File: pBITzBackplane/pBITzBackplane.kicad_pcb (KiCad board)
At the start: 4 copper layers, 243.8 x 243.8 mm, 53 parts, among them J1 ATX-24, J2 pBITzBus, J3 pBITzBus, J4 pBITzBus, J5 pBITzBus, J6 pBITzBus, J7 Conn_02x10_Odd_Even, Q1 BSS138, SW1 SW_Push, U1 ATtiny85-20P

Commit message: Changed the pBITz backplane connector from a PCIe 8x to a DIN 41612 connector.
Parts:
- removed H1: MountingHole, MountingHole:MountingHole_3.5mm_Pad_TopBottom
- removed H10, H11, H12, H13: MountingHole (DB), MountingHole:MountingHole_3.5mm_Pad_TopBottom
- removed H2: MountingHole (C), MountingHole:MountingHole_3.5mm_Pad_TopBottom
- removed H3: MountingHole (J), MountingHole:MountingHole_3.5mm_Pad_TopBottom
- removed H4: MountingHole (S), MountingHole:MountingHole_3.5mm_Pad_TopBottom
- removed H5: MountingHole (R), MountingHole:MountingHole_3.5mm_Pad_TopBottom
- removed H6: MountingHole (B), MountingHole:MountingHole_3.5mm_Pad_TopBottom
- removed H7: MountingHole (M), MountingHole:MountingHole_3.5mm_Pad_TopBottom
- removed H8: MountingHole (H), MountingHole:MountingHole_3.5mm_Pad_TopBottom
- removed H9: MountingHole (L), MountingHole:MountingHole_3.5mm_Pad_TopBottom
- removed J2, J3, J4, J5: pBITzBus, Footprints:AMPHENOL_10018783-10202TLF
- removed RN1, RN2: 4820P-2-472LF, Footprints:SOIC127P762X240-20N
- removed RN3, RN4: 4816P-T02-472LF, Footprints:4816PT02472LF
- added H14: MountingHole_Pad (D), MountingHole:MountingHole_3.5mm_Pad_TopBottom, F.Cu at (182.8, 198.1)
- added H15: MountingHole_Pad (J), MountingHole:MountingHole_3.5mm_Pad_TopBottom, F.Cu at (386.0, 353.1)
- added H16: MountingHole_Pad (R), MountingHole:MountingHole_3.5mm_Pad_TopBottom, F.Cu at (182.8, 353.1)
- added H17: MountingHole_Pad (M), MountingHole:MountingHole_3.5mm_Pad_TopBottom, F.Cu at (293.1, 352.7)
- added H18: MountingHole_Pad (L), MountingHole:MountingHole_3.5mm_Pad_TopBottom, F.Cu at (293.1, 424.1)
- added H19: MountingHole_Pad (DB), MountingHole:MountingHole_3.5mm_Pad_TopBottom, F.Cu at (228.5, 198.1)
- added H20: MountingHole_Pad (DB), MountingHole:MountingHole_3.5mm_Pad_TopBottom, F.Cu at (386.0, 425.4)
- added H21: MountingHole_Pad (C), MountingHole:MountingHole_3.5mm_Pad_TopBottom, F.Cu at (202.2, 352.7)
- added H22: MountingHole_Pad (S), MountingHole:MountingHole_3.5mm_Pad_TopBottom, F.Cu at (228.5, 425.4)
- added H23: MountingHole_Pad (B), MountingHole:MountingHole_3.5mm_Pad_TopBottom, F.Cu at (202.2, 424.1)
- added H24: MountingHole_Pad (H), MountingHole:MountingHole_3.5mm_Pad_TopBottom, F.Cu at (386.0, 221.0)
- added H25: MountingHole_Pad (DB), MountingHole:MountingHole_3.5mm_Pad_TopBottom, F.Cu at (162.5, 353.1)
- added H26: MountingHole_Pad (DB), MountingHole:MountingHole_3.5mm_Pad_TopBottom, F.Cu at (228.5, 353.1)
- added J10: ~, Footprints:AMPHENOL_86093968114T55F1LF, F.Cu at (184.8, 282.5)
- added J11: ~, Footprints:AMPHENOL_86093968114T55F1LF, F.Cu at (164.5, 282.5)
- added J8: ~, Footprints:AMPHENOL_86093968114T55F1LF, F.Cu at (225.5, 282.5)
- added J9: ~, Footprints:AMPHENOL_86093968114T55F1LF, F.Cu at (205.2, 282.5)
- added RN10: 4614X-101-472LF, Resistor_THT:R_Array_SIP14, F.Cu at (240.7, 289.7)
- added RN5: 4614X-101-472LF, Resistor_THT:R_Array_SIP14, F.Cu at (234.3, 253.4)
- added RN6: 4614X-101-472LF, Resistor_THT:R_Array_SIP14, F.Cu at (237.5, 253.4)
- added RN7: 4614X-101-472LF, Resistor_THT:R_Array_SIP14, F.Cu at (240.7, 253.4)
- added RN8: 4614X-101-472LF, Resistor_THT:R_Array_SIP14, F.Cu at (234.3, 289.7)
- added RN9: 4614X-101-472LF, Resistor_THT:R_Array_SIP14, F.Cu at (237.5, 289.7)
- moved C15 55.7 mm to (221.6, 233.0)
- moved C12 46.3 mm to (160.6, 233.0)
- moved C14 25.9 mm to (201.3, 233.0)
- moved J7 13.6 mm to (250.8, 341.4)
- moved C13 7.06 mm to (180.9, 233.0)
- moved C8 5.69 mm to (167.6, 233.0), turned to 0 degrees
- moved C9 5.67 mm to (187.9, 233.0), turned to 0 degrees
- moved C10 5.66 mm to (208.2, 233.0), turned to 0 degrees
- moved C11 5.58 mm to (228.5, 233.0), turned to 0 degrees
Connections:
- net /Backplane/SPI_CD renamed /Backplane/~{SPI_CD}
- net /Backplane/SPI_CS0 renamed /Backplane/~{SPI_CS0}
- net /Backplane/SPI_CS1 renamed /Backplane/~{SPI_CS1}
- J6 pad A5: /Backplane/CLK2 -> unconnected-(J6A-CLK2-PadA5)
- J6 pad A6: /Backplane/CLK3 -> unconnected-(J6A-CLK3-PadA6)
- J6 pad A8: /Backplane/PROG -> /Backplane/~{PROG}
- J6 pad B8: /Backplane/CART -> /Backplane/~{CART}
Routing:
- net /Backplane/CART: track 197.8 -> 0.00 mm, vias 2 -> 0
- net /Backplane/PROG: track 191.3 -> 0.00 mm, vias 2 -> 0
- net /Backplane/~{PROG}: track 0.00 -> 169.6 mm, vias 0 -> 1
- net /Backplane/~{CART}: track 0.00 -> 161.1 mm, vias 0 -> 2
- net /Backplane/CLK3: track 138.2 -> 0.00 mm, vias 1 -> 0
- net /Backplane/CLK2: track 136.6 -> 0.00 mm, vias 1 -> 0
- net +3V3: track 544.4 -> 594.9 mm
- net /Backplane/~{SHUTDOWN_RQ}: track 314.6 -> 359.4 mm, vias 1 -> 2
- net /Backplane/~{PWR_OFF}: track 323.2 -> 360.7 mm, vias 1 -> 2
- net /Backplane/CTRL_2: track 206.1 -> 168.7 mm, vias 2 -> 0
- net /Backplane/CTRL_5: track 208.3 -> 171.9 mm, vias 2 -> 0
- net /Backplane/CTRL_1: track 204.5 -> 169.6 mm, vias 2 -> 1
- net /Backplane/A22: track 234.4 -> 267.5 mm, vias 2 -> 1
- net /Backplane/A21: track 235.2 -> 268.1 mm, vias 2 -> 1
- net /Backplane/~{RESET}: track 202.0 -> 169.6 mm, vias 2 -> 1
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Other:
- board text added: "Mezzanine Card When attached to backplane use Holes H17, H18, H21, H23"
- board text removed: "3V3"
- board text removed: "5V"
- board text removed: "A12"
- board text removed: "A20"
- board text removed: "A23"
- board text removed: "CS2"
- board text removed: "CTRL0"
- board text removed: "CTRL11"
- board text removed: "CTRL19"
- board text removed: "CTRL9"
- board text removed: "D15"
- board text removed: "D8"
- board text removed: "Mezzanine Card When attached to backplane use Holes H10-H13"
- board text removed: "Mezzanine Connector"
- board text removed: "SPI"

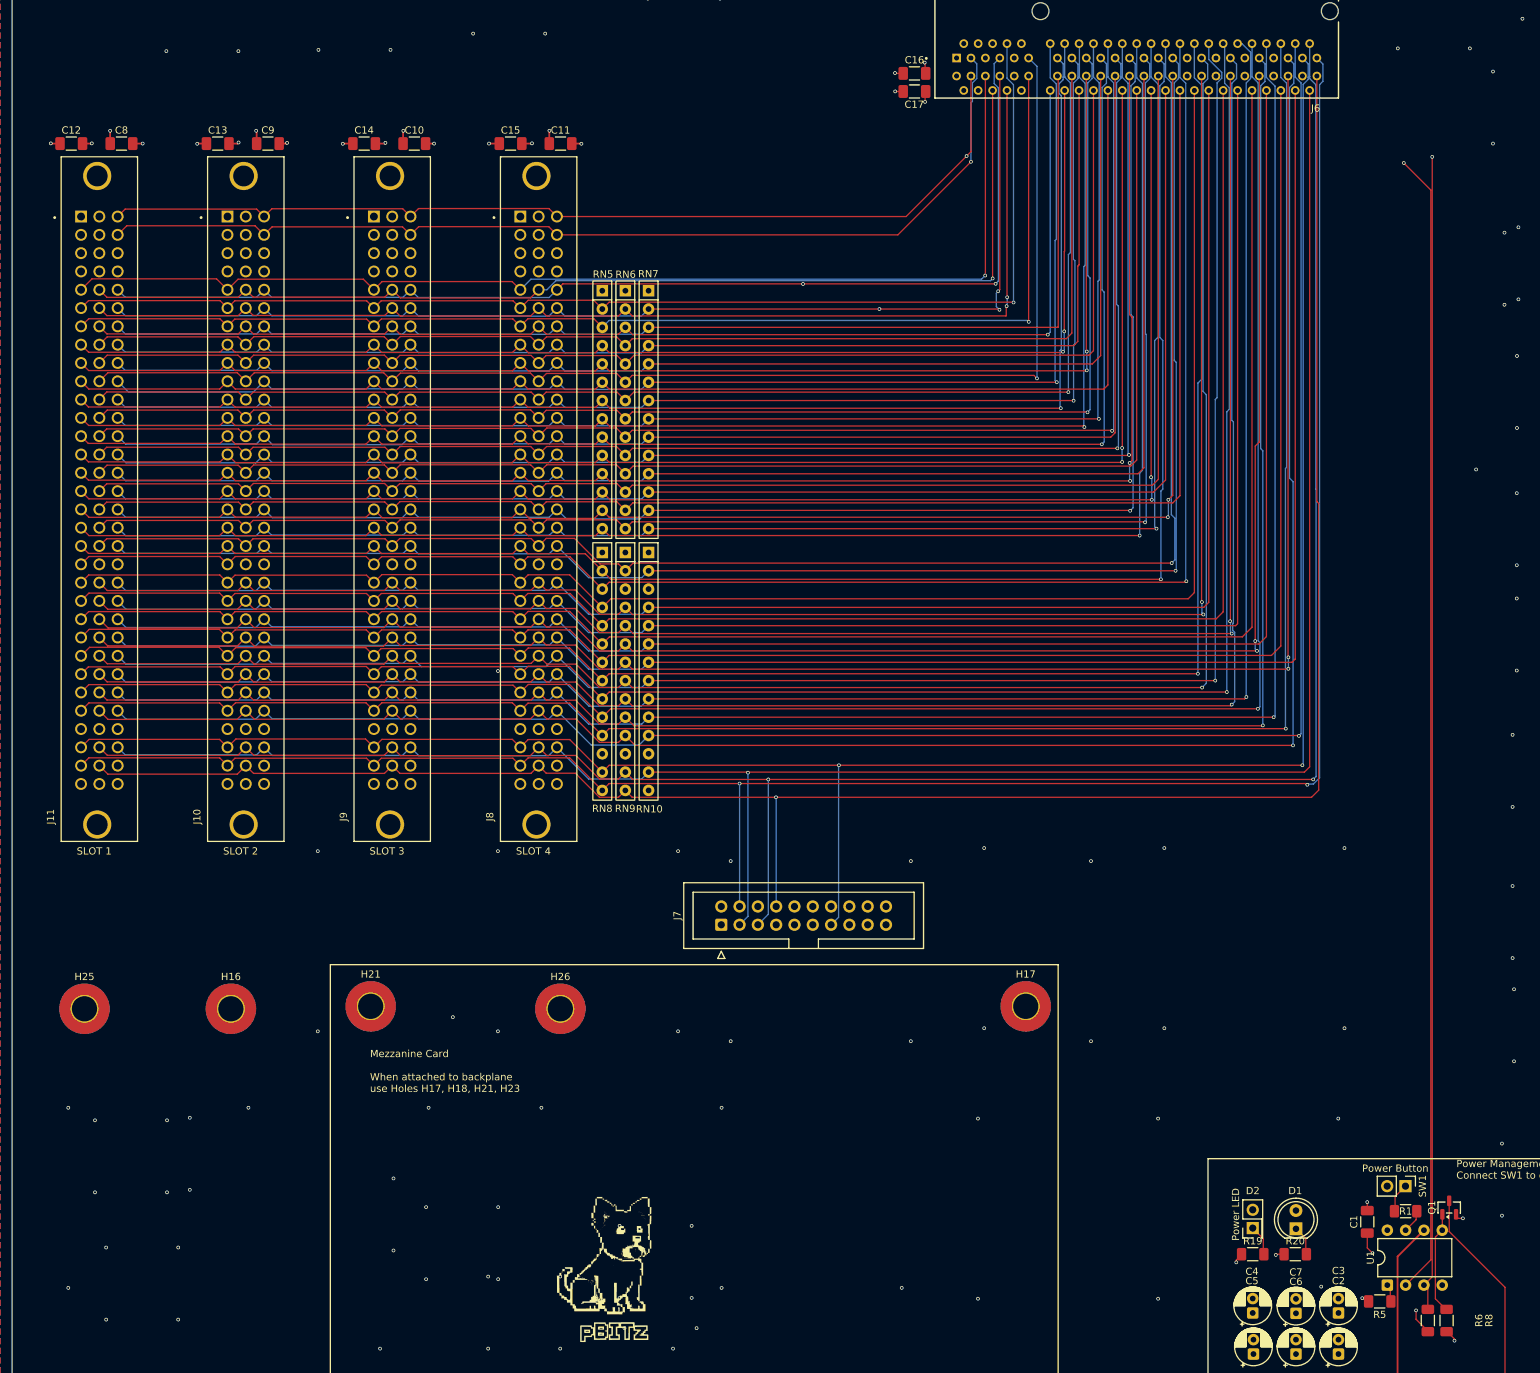
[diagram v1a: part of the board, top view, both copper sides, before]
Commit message: Moved to the DIN Connector
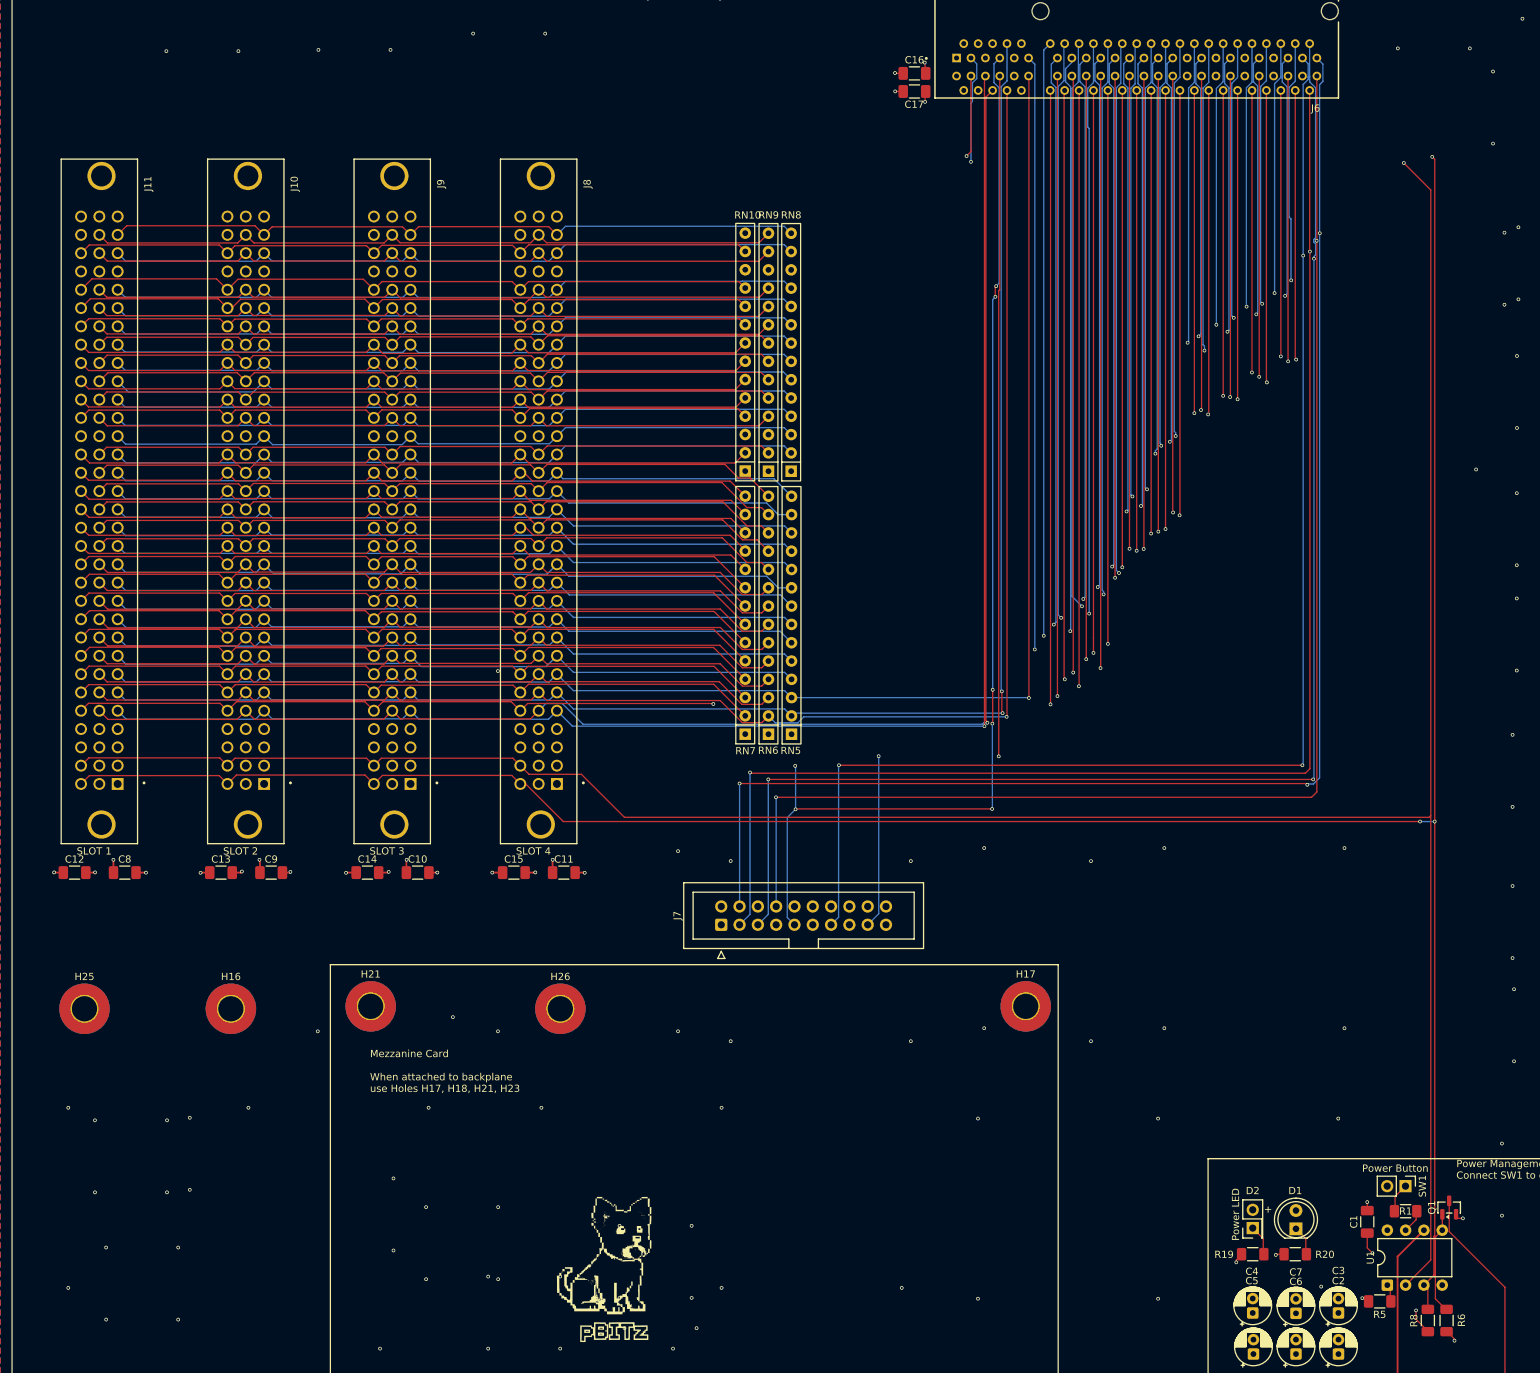
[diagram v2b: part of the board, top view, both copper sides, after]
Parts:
- moved C10 101.2 mm to (208.7, 334.2)
- moved C11 101.2 mm to (229.0, 334.2)
- moved C12 101.2 mm to (161.1, 334.2)
- moved C13 101.2 mm to (181.4, 334.2)
- moved C14 101.2 mm to (201.7, 334.2)
- moved C15 101.2 mm to (222.0, 334.2)
- moved C8 101.2 mm to (168.0, 334.2)
- moved C9 101.2 mm to (188.4, 334.2)
- moved RN5 66.9 mm to (260.6, 315.0), turned to 90 degrees
- moved RN6 64.7 mm to (257.4, 315.0), turned to 90 degrees
- moved RN7 63.0 mm to (254.1, 314.9), turned to 90 degrees
- moved RN8 28.5 mm to (260.5, 278.5), turned to 90 degrees
- moved RN9 22.8 mm to (257.4, 278.5), turned to 90 degrees
- moved RN10 17.5 mm to (254.1, 278.4), turned to 90 degrees
- turned J10 to -90 degrees
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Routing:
- net /Backplane/MOSI: track 286.1 -> 368.7 mm, vias 1 -> 2
- net /Backplane/MISO: track 297.3 -> 371.9 mm, vias 2 -> 3
- net /Backplane/~{SPI_CS0}: track 295.2 -> 369.1 mm, vias 2 -> 3
- net /Backplane/~{SPI_CS1}: track 289.4 -> 363.0 mm, vias 1 -> 2
- net /Backplane/~{PWR_OFF}: track 360.7 -> 430.0 mm, vias 2 -> 4
- net /Backplane/A21: track 268.1 -> 199.5 mm
- net /Backplane/~{SHUTDOWN_RQ}: track 359.4 -> 426.9 mm
- net /Backplane/A22: track 267.5 -> 202.8 mm
- net /Backplane/A18: track 261.7 -> 197.1 mm
- net /Backplane/CLK1: track 153.4 -> 216.1 mm
- net /Backplane/A23: track 265.8 -> 206.3 mm
- net /Backplane/A19: track 260.1 -> 200.9 mm
- net /Backplane/A15: track 254.5 -> 195.4 mm
- net /Backplane/CTRL_2: track 168.7 -> 227.3 mm, vias 0 -> 1
- net /Backplane/~{SPI_INT}: track 296.4 -> 354.3 mm, vias 2 -> 3
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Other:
- board text added: "+"
